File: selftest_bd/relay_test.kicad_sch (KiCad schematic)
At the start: 60 parts, among them K14 TQ2-5_Split, K15 TQ2-5_Split

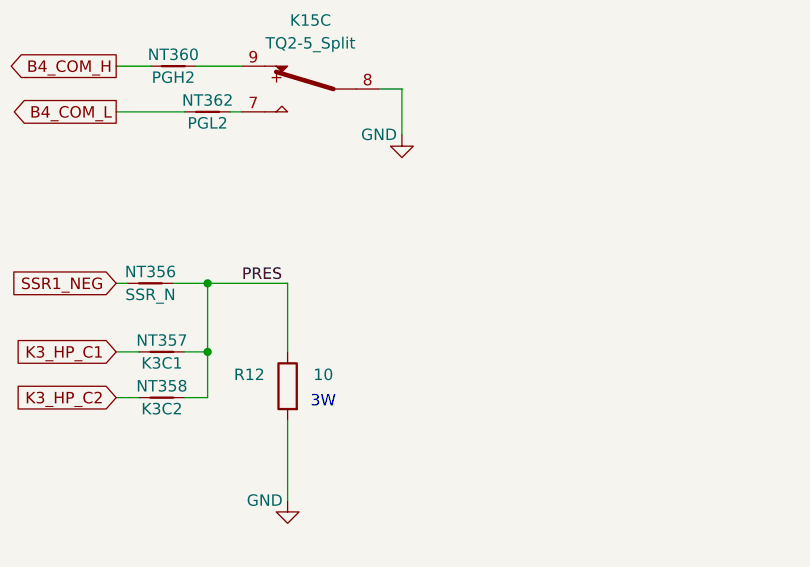
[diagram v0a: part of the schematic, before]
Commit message: Commit V2.0
Redo PCB due to incorrect position of J1 and J2
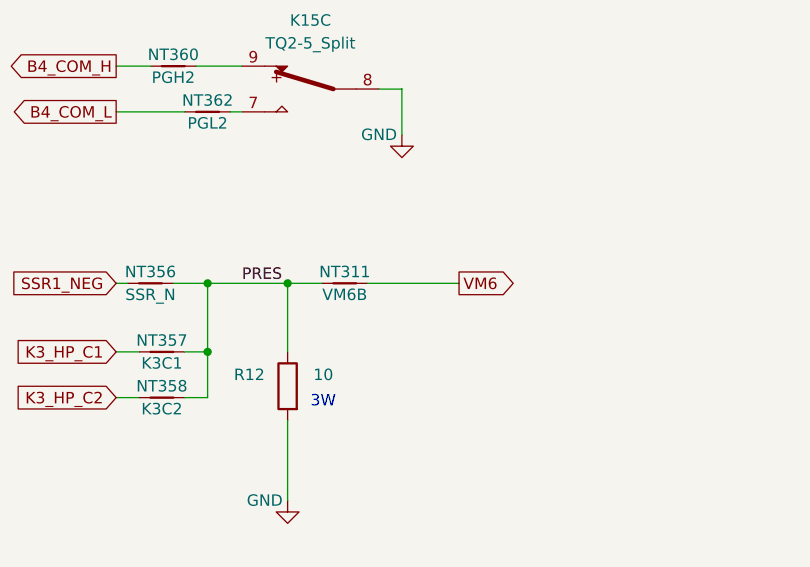
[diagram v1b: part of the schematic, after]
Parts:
- added NT311: VM6B, NetTie:NetTie-2_Front1.0mm, symbol Library:NetTie_2
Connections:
- net PRES: now also NT311.1
- new net VM6: NT311.2
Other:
- title: FIRST TEST STATION SELFTEST BOARD 640-1010-010 -> FIRST TEST STATION SELFTEST BOARD 640-1010-020
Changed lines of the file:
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@@
   (paper "A")
   (title_block
-    (title "FIRST TEST STATION SELFTEST BOARD 640-1010-010")
-    (date "2023-05-16")
-    (rev "1.0")
+    (title "FIRST TEST STATION SELFTEST BOARD 640-1010-020")
+    (date "2023-10-01")
+    (rev "2.0")
+  )
+  (junction (at 106.68 127) (diameter 0) (color 0 0 0 0)
   )
   (junction (at 97.79 134.62) (diameter 0) (color 0 0 0 0)
@@
     (stroke (width 0) (type default))
   )
+  (wire (pts (xy 115.57 127) (xy 125.73 127))
+    (stroke (width 0) (type default))
+  )
   (wire (pts (xy 85.09 52.07) (xy 96.52 52.07))
     (stroke (width 0) (type default))
@@
   )
   (wire (pts (xy 34.29 62.23) (xy 38.1 62.23))
+    (stroke (width 0) (type default))
+  )
+  (wire (pts (xy 106.68 127) (xy 110.49 127))
     (stroke (width 0) (type default))
   )
@@
     )
   )
+  (global_label "VM6" (shape output) (at 125.73 127 0) (fields_autoplaced)
+    (effects (font (size 1.27 1.27)) (justify left))
+    (property "Intersheetrefs" "${INTERSHEET_REFS}" (at 132.3853 127 0)
+      (effects (font (size 1.27 1.27)) (justify left) hide)
+    )
+  )
   (global_label "B35_H" (shape input) (at 85.09 55.88 180) (fields_autoplaced)
     (effects (font (size 1.27 1.27)) (justify right))
@@
         )
       )
+    )
+  )
+  (symbol (lib_id "Library:NetTie_2") (at 113.03 127 0) (unit 1)
+    (in_bom yes) (on_board yes) (dnp no)
+    (property "Reference" "NT311" (at 113.03 125.73 0)
+      (effects (font (size 1.27 1.27)))
+    )
+    (property "Value" "VM6B" (at 113.03 128.27 0)
+      (effects (font (size 1.27 1.27)))
+    )
+    (property "Footprint" "NetTie:NetTie-2_Front1.0mm" (at 113.03 127 0)
+      (effects (font (size 1.27 1.27)) hide)
+    )
+    (property "Datasheet" "~" (at 113.03 127 0)
+      (effects (font (size 1.27 1.27)) hide)
+    )
+    (pin "1")
+    (pin "2")
+    (instances
+      (project "selftest_bd"
+        (path "/e63e39d7-6ac0-4ffd-8aa3-1841a4541b55/0804e938-ad61-40c0-a804-2ce216de69d1"
+          (reference "NT311") (unit 1)
+        )
+        (path "/e63e39d7-6ac0-4ffd-8aa3-1841a4541b55/c667817b-67e3-46ac-b45b-0a9eaacadd99"
+          (reference "NT311") (unit 1)
+        )
+      )

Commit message: update README and small correction
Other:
- title: FIRST TEST STATION SELFTEST BOARD 640-1010-020 -> FIRST TEST STATION SELFTEST BOARD 640-1010-021
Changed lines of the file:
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@@
   (paper "A")
   (title_block
-    (title "FIRST TEST STATION SELFTEST BOARD 640-1010-020")
+    (title "FIRST TEST STATION SELFTEST BOARD 640-1010-021")
     (date "2023-10-01")
-    (rev "2.0")
+    (rev "2.1")
   )
   (junction (at 106.68 127) (diameter 0) (color 0 0 0 0)

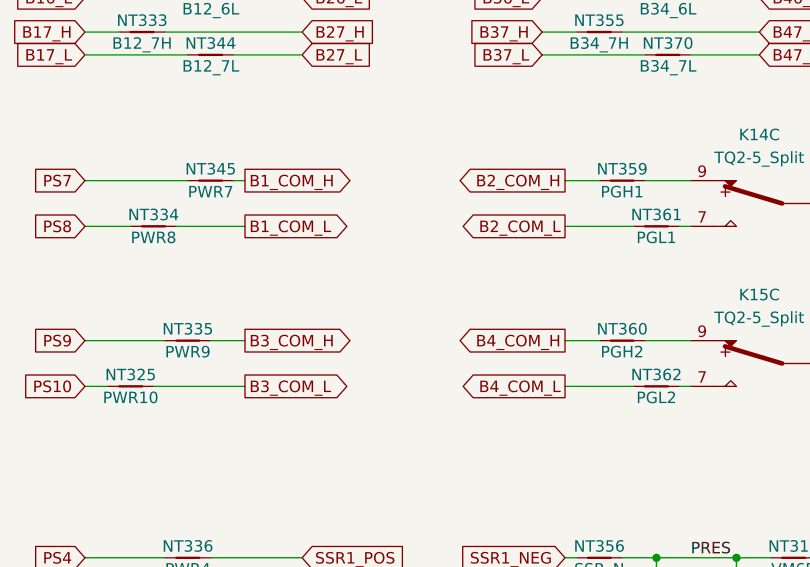
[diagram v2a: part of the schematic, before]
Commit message: Reverse COM_H and COM_L on relay Bank
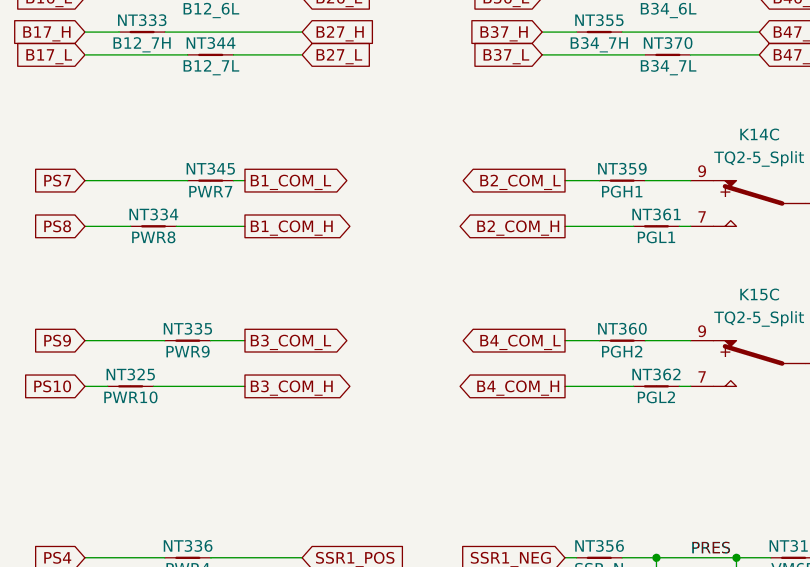
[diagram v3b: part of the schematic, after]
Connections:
- net B1_COM_H: now also NT334.1; no longer NT345.1
- net B1_COM_L: now also NT345.1; no longer NT334.1
- net B2_COM_H: now also NT361.2; no longer NT359.2
- net B2_COM_L: now also NT359.2; no longer NT361.2
- net B3_COM_H: now also NT325.1; no longer NT335.1
- net B3_COM_L: now also NT335.1; no longer NT325.1
- net B4_COM_H: now also NT362.2; no longer NT360.2
- net B4_COM_L: now also NT360.2; no longer NT362.2
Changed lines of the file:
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@@
     )
   )
-  (global_label "B3_COM_H" (shape output) (at 52.07 102.87 0) (fields_autoplaced)
-    (effects (font (size 1.27 1.27)) (justify left))
-    (property "Intersheetrefs" "${INTERSHEET_REFS}" (at 64.2802 102.7906 0)
+  (global_label "B3_COM_L" (shape output) (at 52.07 102.87 0) (fields_autoplaced)
+    (effects (font (size 1.27 1.27)) (justify left))
+    (property "Intersheetrefs" "${INTERSHEET_REFS}" (at 64.4705 102.87 0)
       (effects (font (size 1.27 1.27)) (justify left) hide)
     )
@@
     )
   )
-  (global_label "B3_COM_L" (shape output) (at 52.07 107.95 0) (fields_autoplaced)
-    (effects (font (size 1.27 1.27)) (justify left))
-    (property "Intersheetrefs" "${INTERSHEET_REFS}" (at 63.9779 107.8706 0)
+  (global_label "B3_COM_H" (shape output) (at 52.07 107.95 0) (fields_autoplaced)
+    (effects (font (size 1.27 1.27)) (justify left))
+    (property "Intersheetrefs" "${INTERSHEET_REFS}" (at 64.7729 107.95 0)
       (effects (font (size 1.27 1.27)) (justify left) hide)
     )
@@
     )
   )
-  (global_label "B2_COM_L" (shape output) (at 87.63 90.17 180) (fields_autoplaced)
-    (effects (font (size 1.27 1.27)) (justify right))
-    (property "Intersheetrefs" "${INTERSHEET_REFS}" (at 75.7221 90.0906 0)
+  (global_label "B2_COM_H" (shape output) (at 87.63 90.17 180) (fields_autoplaced)
+    (effects (font (size 1.27 1.27)) (justify right))
+    (property "Intersheetrefs" "${INTERSHEET_REFS}" (at 74.9271 90.17 0)
       (effects (font (size 1.27 1.27)) (justify right) hide)
     )
@@
     )
   )
-  (global_label "B1_COM_L" (shape output) (at 52.07 90.17 0) (fields_autoplaced)
-    (effects (font (size 1.27 1.27)) (justify left))
-    (property "Intersheetrefs" "${INTERSHEET_REFS}" (at 63.9779 90.0906 0)
+  (global_label "B1_COM_H" (shape output) (at 52.07 90.17 0) (fields_autoplaced)
+    (effects (font (size 1.27 1.27)) (justify left))
+    (property "Intersheetrefs" "${INTERSHEET_REFS}" (at 64.7729 90.17 0)
       (effects (font (size 1.27 1.27)) (justify left) hide)
     )
@@
     )
   )
-  (global_label "B1_COM_H" (shape output) (at 52.07 85.09 0) (fields_autoplaced)
-    (effects (font (size 1.27 1.27)) (justify left))
-    (property "Intersheetrefs" "${INTERSHEET_REFS}" (at 64.2802 85.0106 0)
+  (global_label "B1_COM_L" (shape output) (at 52.07 85.09 0) (fields_autoplaced)
+    (effects (font (size 1.27 1.27)) (justify left))
+    (property "Intersheetrefs" "${INTERSHEET_REFS}" (at 64.4705 85.09 0)
       (effects (font (size 1.27 1.27)) (justify left) hide)
     )
@@
     )
   )
-  (global_label "B4_COM_H" (shape output) (at 87.63 102.87 180) (fields_autoplaced)
-    (effects (font (size 1.27 1.27)) (justify right))
-    (property "Intersheetrefs" "${INTERSHEET_REFS}" (at 75.4198 102.7906 0)
+  (global_label "B4_COM_L" (shape output) (at 87.63 102.87 180) (fields_autoplaced)
+    (effects (font (size 1.27 1.27)) (justify right))
+    (property "Intersheetrefs" "${INTERSHEET_REFS}" (at 75.2295 102.87 0)
       (effects (font (size 1.27 1.27)) (justify right) hide)
     )
@@
     )
   )
-  (global_label "B4_COM_L" (shape output) (at 87.63 107.95 180) (fields_autoplaced)
-    (effects (font (size 1.27 1.27)) (justify right))
-    (property "Intersheetrefs" "${INTERSHEET_REFS}" (at 75.7221 107.8706 0)
+  (global_label "B4_COM_H" (shape output) (at 87.63 107.95 180) (fields_autoplaced)
+    (effects (font (size 1.27 1.27)) (justify right))
+    (property "Intersheetrefs" "${INTERSHEET_REFS}" (at 74.9271 107.95 0)
       (effects (font (size 1.27 1.27)) (justify right) hide)
     )
@@
     )
   )
-  (global_label "B2_COM_H" (shape output) (at 87.63 85.09 180) (fields_autoplaced)
-    (effects (font (size 1.27 1.27)) (justify right))
-    (property "Intersheetrefs" "${INTERSHEET_REFS}" (at 75.4198 85.0106 0)
-      (effects (font (size 1.27 1.27)) (justify right) hide)
-    )
+  (global_label "B2_COM_L" (shape output) (at 87.63 85.09 180) (fields_autoplaced)
+    (effects (font (size 1.27 1.27)) (justify right))
+    (property "Intersheetrefs" "${INTERSHEET_REFS}" (at 75.2295 85.09 0)
+      (effects (font (size 1.27 1.27)) (justify right) hide)
+    )
